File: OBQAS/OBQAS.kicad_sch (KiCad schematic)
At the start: 41 parts

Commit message: continued schematic editing
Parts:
- removed U?: Pico, RPi_Pico:RPi_Pico_SMD_TH, symbol MCU_RaspberryPi_and_Boards:Pico
- added C?: 220u, symbol Device:C_Polarized
- added C?: 100p, symbol Device:C
- added C? (x2): 10u, symbol Device:C
- added C?: 100n, symbol Device:C
- added D? (x4): 1N4001, Diode_THT:D_DO-41_SOD81_P10.16mm_Horizontal, symbol Diode:1N4001
- added J?: CH2, symbol Connector:Conn_01x02_Female
- added J?: CH1, symbol Connector:Conn_01x02_Female
- added J?: USB_C_Receptacle_USB2.0, symbol Connector:USB_C_Receptacle_USB2.0
- added K? (x4): G5NB-1A-E_DC5, RELAY_G5NB-1A DC5_OMR, symbol 2022-01-22_12-19-34:G5NB-1A-E_DC5
- added Q? (x4): IRLML2803TRPBF, SOT95P237X112-3N, symbol IRLML2803TRPBF:IRLML2803TRPBF
- added Q? (x2): BC846, Package_TO_SOT_SMD:SOT-23, symbol Transistor_BJT:BC846
- added R? (x14): 10k, symbol Device:R
- added R?: 1k, symbol Device:R
- added R? (x2): 50k, symbol Device:R
- added R? (x4): 100k, symbol Device:R
- added R? (x6): 470, symbol Device:R
- added R?: 5.1k(NC), symbol Device:R
- added R?: 1M, symbol Device:R
- added R?: 100mOhm, symbol Device:R
- added R? (x4): 2k, symbol Device:R
- added R? (x2): 10mOhm, symbol Device:R
- added R? (x2): 5.1k, symbol Device:R
- added R?: 0, symbol Device:R
- added SW?: SW_SPDT, symbol Switch:SW_SPDT
- added U? (x6): LM358, symbol Amplifier_Operational:LM358
- added U?: ESP32-WROOM-32, RF_Module:ESP32-WROOM-32, symbol RF_Module:ESP32-WROOM-32
- added U?: ADS1115IDGS, Package_SO:TSSOP-10_3x3mm_P0.5mm, symbol Analog_ADC:ADS1115IDGS
- added U?: AMS1117-3.3, Package_TO_SOT_SMD:SOT-223-3_TabPin2, symbol Regulator_Linear:AMS1117-3.3
- added U?: CH340C, Package_SO:SOIC-16_3.9x9.9mm_P1.27mm, symbol Interface_USB:CH340C
- added U?: ESP32-S2-WROVER-I, RF_Module:ESP32-S2-WROVER, symbol RF_Module:ESP32-S2-WROVER-I
- added U?: MCP4921, symbol Analog_DAC:MCP4921
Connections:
- net EN: now also C?.1, Q?.3 (C), R?.1, U?.3 (EN)
- net GND: now also U?.2 (GND), C?.1, C?.2, C?.2, C?.2, C?.2, D?.2 (A), D?.2 (A), D?.2 (A), D?.2 (A), J?.2 (Pin_2), J?.2 (Pin_2), J?.A1 (GND), J?.A12 (GND), J?.B1 (GND), J?.B12 (GND), J?.S1 (SHIELD), K?.1, K?.1, K?.4, K?.4, Q?.2, Q?.2, Q?.2, Q?.2, R?.1, R?.1, R?.1, R?.1, R?.1, R?.1, R?.1, R?.1, R?.2, R?.2, R?.2, R?.2, U?.1 (GND), U?.1 (GND), U?.1 (GND), U?.15 (GND), U?.3 (GND), U?.38 (GND), U?.39 (GND), U?.4 (V-), U?.4 (V-), U?.7 (Vss)
- net SCL: now also U?.10 (SCL)
- net SDA: now also U?.9 (SDA)
- net TPS_OUT: now also K?.3, K?.3
- net VCC: now also U?.1 (VI), SW?.1 (A); no longer J?.1
- net at Q?.1 (G): now also R?.2, R?.2
- net LOAD_IN: now reaches Q?.2 (D)
- net LOAD_IN: now also K?.3, K?.3
- net at Q?.3 (S): now also R?.2, R?.2
- net +5V: now reaches U?.3 (VO)
- net +5V: now also C?.1, J?.A4 (VBUS), J?.A9 (VBUS), J?.B4 (VBUS), J?.B9 (VBUS), R?.1, U?.16 (VCC), U?.3 (VI), U?.8 (V+), U?.8 (V+), U?.8 (VDD)
- new net: Q?.1, R?.2, R?.2 (x4)
- new net: Q?.2 (E), R?.1, U?.13 (~{DTR})
- new net: Q?.1 (B), R?.2 (x2)
- new net: R?.1, R?.1, U?.2 (-)
- new net: R?.1, R?.2, U?.1
- new net: R?.2, R?.2, R?.2, U?.3 (+)
- new net: K?.2, K?.2, R?.1, R?.2, R?.2 (x2)
- new net: J?.1 (Pin_1), R?.2, R?.2 (x2)
- new net: R?.1, R?.2, U?.3 (+)
- new net: J?.1, SW?.2 (B)
- new net: R?.1, R?.2, U?.2 (-)
- new net: R?.1, R?.1, U?.8 (Vout)
- new net: R?.1, R?.2, U?.5 (+)
- new net: J?.A5 (CC1), R?.1
- new net: R?.1, R?.2, U?.6 (-)
- new net: Q?.2 (E), R?.1, U?.14 (~{RTS})
- new net: R?.1, U?.2 (TXD)
- new net: J?.A6 (D+), J?.B6 (D+), U?.5 (UD+)
- new net: J?.A7 (D-), J?.B7 (D-), U?.6 (UD-)
- new net: U?.1 (GND), U?.26 (GND), U?.42 (GND), U?.43 (GND)
- new net: J?.B5 (CC2), R?.1
- new net +2V5: R?.1, R?.1, R?.1, R?.2
- new net +3V3: C?.1, C?.1, C?.2, R?.2, R?.2, U?.1 (Vdd), U?.2 (VDD), U?.2 (VO), U?.4 (V3), U?.6 (Vref)
- new net CH1R1: D?.1 (K), K?.4, Q?.3
- new net CH1R1_SIG: R?.1
- new net CH1R2: D?.1 (K), K?.1, Q?.3
- new net CH1R2_SIG: R?.1
- new net CH1_ADC_I: R?.1, U?.6 (AIN2), U?.7
- new net CH1_ADC_V: R?.1, R?.1, U?.4 (AIN0)
- new net CH2R1: D?.1 (K), K?.4, Q?.3
- new net CH2R1_SIG: R?.1
- new net CH2R2: D?.1 (K), K?.1, Q?.3
- new net CH2R2_SIG: R?.1
- new net CH2_ADC_I: R?.1, U?.1, U?.7 (AIN3)
- new net CH2_ADC_V: R?.1, R?.2, U?.5 (AIN1)
- new net IO0: Q?.3 (C), R?.1, U?.25 (IO0)
- new net RX: U?.3 (RXD)
- new net TX: R?.2
- no-connect marks 0 -> 7
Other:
- moved on the sheet: U?

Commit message: Finished schematic
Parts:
- removed U?: ESP32-S2-WROVER-I, RF_Module:ESP32-S2-WROVER, symbol RF_Module:ESP32-S2-WROVER-I
- added C19, C20: 100n, Capacitor_SMD:C_0805_2012Metric_Pad1.18x1.45mm_HandSolder, symbol Device:C
- added D1: LED, LED_SMD:LED_1206_3216Metric_Pad1.42x1.75mm_HandSolder, symbol Device:LED
- added DISP1: LCD, LCD:LCD-20x4, symbol Connector:Conn_01x04_Female
- added J3: K type, TerminalBlock:TerminalBlock_Altech_AK300-2_P5.00mm, symbol Connector:Screw_Terminal_01x02
- added J5: Micro_SD_Card, symbol Connector:Micro_SD_Card
- added R15: 1k, symbol Device:R
- added R20, R21, R22: 10k, symbol Device:R
- added R35, R40, R46, R52, R58: 49.9k, symbol Device:R
- added R9: 470, symbol Device:R
- added TP1: SENS_VP, symbol Connector:TestPoint
- added TP10: SCL, symbol Connector:TestPoint
- added TP11: SDA, symbol Connector:TestPoint
- added TP2: SENS_VN, symbol Connector:TestPoint
- added TP3: +5V, symbol Connector:TestPoint
- added TP4: +3V3, symbol Connector:TestPoint
- added TP5: IO0, symbol Connector:TestPoint
- added TP6: EN, symbol Connector:TestPoint
- added TP7: RX, symbol Connector:TestPoint
- added TP8: TX, symbol Connector:TestPoint
- added TP9: ADC_READY, symbol Connector:TestPoint
- C1, C15, C16, C18, C2, C8: renamed from C?; footprint (none) -> Capacitor_SMD:C_1206_3216Metric_Pad1.33x1.80mm_HandSolder
- C10, C11, C13, C14, C17, C4, C5, C9: renamed from C?; footprint (none) -> Capacitor_SMD:C_0805_2012Metric_Pad1.18x1.45mm_HandSolder
- C12: renamed from C?; footprint (none) -> Capacitor_SMD:C_1210_3225Metric_Pad1.33x2.70mm_HandSolder
- C3: renamed from C?; footprint (none) -> Capacitor_SMD:CP_Elec_6.3x9.9
- C6: renamed from C?; footprint (none) -> Capacitor_SMD:CP_Elec_10x10
- C7: renamed from C?; footprint (none) -> Capacitor_SMD:CP_Elec_8x6.9
- J1: renamed from J?; footprint (none) -> Connector_AMASS:AMASS_XT60-F_1x02_P7.20mm_Vertical
- J2: renamed from J?; footprint (none) -> Connector_USB:USB_C_Receptacle_Palconn_UTC16-G
- K1, K2, K3, K4: renamed from K?; footprint RELAY_G5NB-1A DC5_OMR -> (none)
- Q1, Q2, Q3, Q4: renamed from Q?; footprint SOT95P237X112-3N -> (none)
- U5: renamed from U?; footprint RPM0026A-MFG -> (none)
- gave numbers to parts that had none: 80
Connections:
- net +2V5: now also U6.5 (+)
- net +3V3: now also C20.2, J5.4 (VDD), R20.2, R21.2, R22.2, R35.2, R40.2, R46.2, R52.2, R58.2, TP4.1
- net +5V: now also C19.1, DISP1.2 (Pin_2), TP3.1
- net CH1R1_SIG: now also U3.9 (IO33)
- net CH1R2_SIG: now also U3.8 (IO32)
- net CH2R1_SIG: now also U3.12 (IO27)
- net CH2R2_SIG: now also U3.11 (IO26)
- net EN: now also TP6.1
- net GND: now also U3.4 (SENSOR_VP), U9.1 (ADDR), C19.2, C20.1, D1.1 (K), DISP1.1 (Pin_1), J3.2 (Pin_2), J5.6 (VSS), J5.9 (SHIELD), TP1.1
- net IO0: now also TP5.1
- net RX: now also U3.35 (TXD0/IO1), TP7.1
- net SCL: now also U3.36 (IO22), DISP1.4 (Pin_4), R20.1, TP10.1
- net SDA: now also U3.33 (IO21), DISP1.3 (Pin_3), R21.1, TP11.1
- net TX: now also U3.34 (RXD0/IO3), TP8.1
- net at U6.6 (-): now also U6.7
- net HSPI_CLK: now reaches U3.13 (IO14)
- net HSPI_CLK: now also U8.3 (SCK)
- net HSPI_MOSI: now reaches U3.16 (IO13)
- net HSPI_MOSI: now also U8.4 (SDI)
- net HSPI_CS: now reaches U3.23 (IO15)
- net HSPI_CS: now also U8.2 (~{CS})
- net at U3.24 (IO2): now also R9.1
- net ADC_READY: now reaches U3.26 (IO4)
- net ADC_READY: now also U9.2 (ALERT/RDY), R22.1, TP9.1
- net DAC_LDAC: now reaches U3.27 (IO16)
- net DAC_LDAC: now also U8.5 (~{LDAC})
- net SD_SS: now reaches U3.29 (IO5)
- net SD_SS: now also J5.2 (DAT3/CD), R40.1
- net SD_CLK: now reaches U3.30 (IO18)
- net SD_CLK: now also J5.5 (CLK)
- net SD_MISO: now reaches U3.31 (IO19)
- net SD_MISO: now also J5.7 (DAT0), R52.1
- net SD_MOSI: now reaches U3.37 (IO23)
- net SD_MOSI: now also J5.3 (CMD), R46.1
- net TC_-: now reaches U3.5 (SENSOR_VN)
- net TC_-: now also R15.1, TP2.1
- new net: D1.2 (A), R9.2
- new net: J3.1 (Pin_1), R15.2
- new net: J5.8 (DAT1), R58.1
- new net: J5.1 (DAT2), R35.1
- no-connect marks 7 -> 19
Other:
- moved on the sheet: C2, C4, C5, J2, Q1, Q2, Q3, Q4, Q5, Q6, Q9, R1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

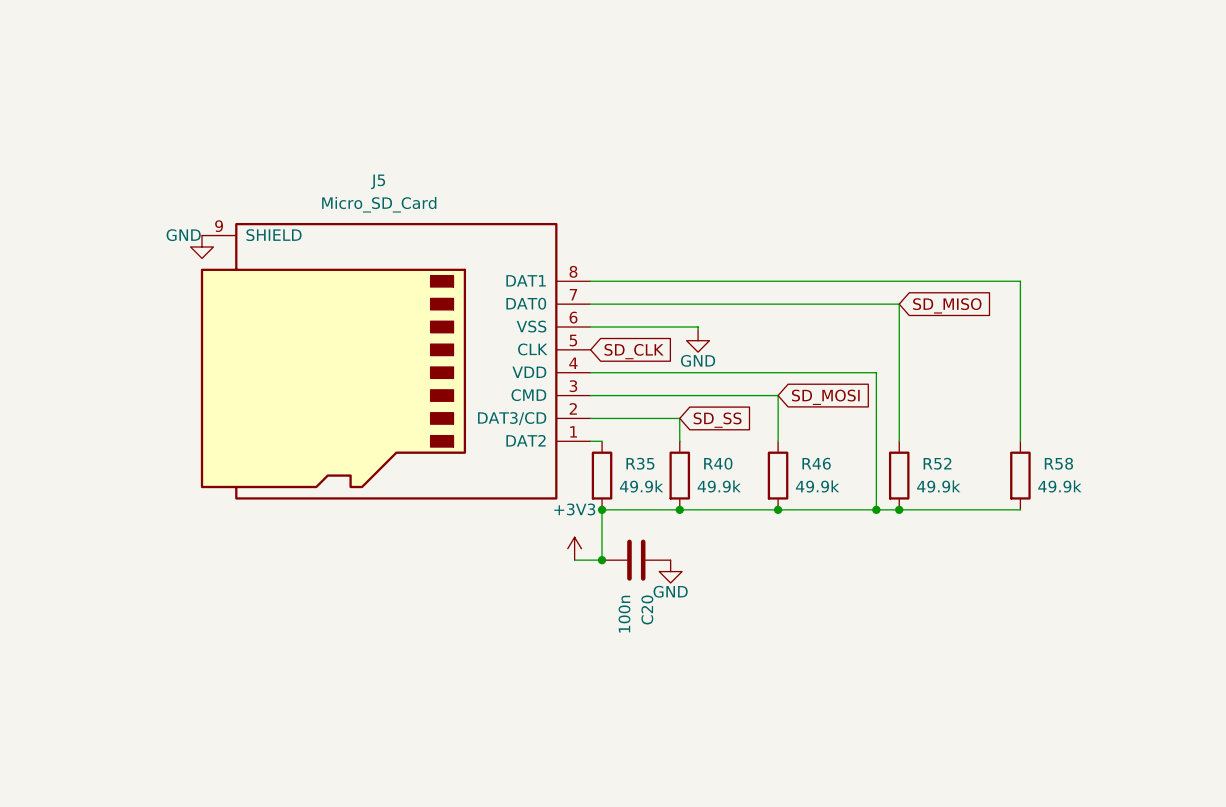
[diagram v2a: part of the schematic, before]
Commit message: changed SD card
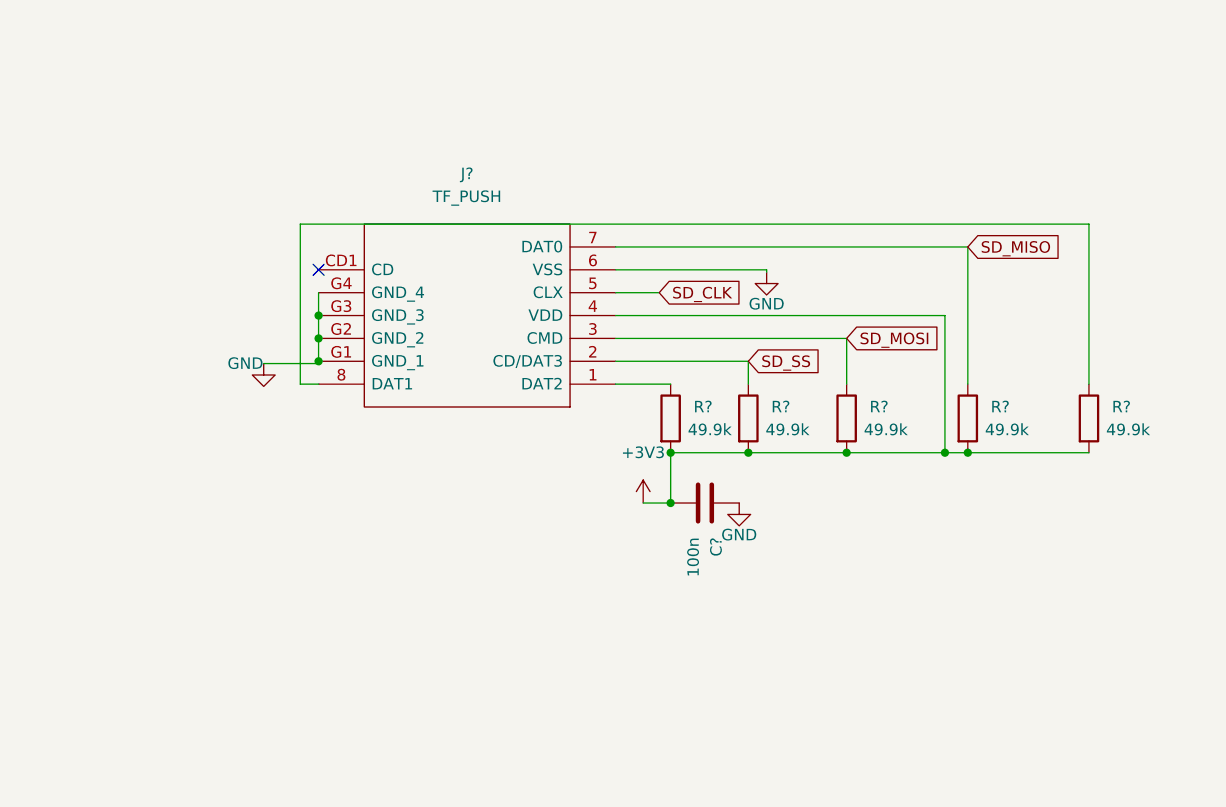
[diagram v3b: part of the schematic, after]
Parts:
- removed C20: 100n, Capacitor_SMD:C_0805_2012Metric_Pad1.18x1.45mm_HandSolder, symbol Device:C
- removed J5: Micro_SD_Card, symbol Connector:Micro_SD_Card
- removed R35, R40, R46, R52, R58: 49.9k, symbol Device:R
- added C?: 100n, Capacitor_SMD:C_0805_2012Metric_Pad1.18x1.45mm_HandSolder, symbol Device:C
- added J?: TF_PUSH, TFPUSH, symbol TF_PUSH:TF_PUSH
- added R? (x5): 49.9k, symbol Device:R
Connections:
- net +3V3: now also C?.2, J?.4 (VDD), R?.2, R?.2, R?.2, R?.2, R?.2
- net GND: now also C?.1, J?.6 (VSS), J?.G1 (GND_1), J?.G2 (GND_2), J?.G3 (GND_3), J?.G4 (GND_4)
- net SD_CLK: now also J?.5 (CLX)
- net SD_MISO: now also J?.7 (DAT0), R?.1
- net SD_MOSI: now also J?.3 (CMD), R?.1
- net SD_SS: now also J?.2 (CD/DAT3), R?.1
- new net: J?.8 (DAT1), R?.1
- new net: J?.1 (DAT2), R?.1
- no-connect marks 19 -> 20

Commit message: added encoder and assigned some footprints
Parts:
- added R? (x3): 10k, Resistor_SMD:R_0805_2012Metric_Pad1.20x1.40mm_HandSolder, symbol Device:R
- added SW2: Enc, symbol Device:RotaryEncoder_Switch
- J5: renamed from J?; footprint TFPUSH -> SD:TFPUSH
- J6, J7: footprint (none) -> TerminalBlock:TerminalBlock_Altech_AK300-2_P5.00mm
- JP1: footprint (none) -> Jumper:SolderJumper-3_P1.3mm_Bridged12_RoundedPad1.0x1.5mm
- K1, K2, K3, K4: footprint (none) -> footprints:G5NB-1A-E DC5
- L1: value L_Iron -> 4.7uH; footprint (none) -> Inductor_THT:L_Radial_D29.8mm_P29.30mm_Murata_1400series
- Q1, Q2, Q3, Q4: footprint (none) -> Package_TO_SOT_SMD:SOT-23
- Q7, Q8: footprint Package_TO_SOT_THT:TO-220-3_Vertical -> Package_TO_SOT_THT:TO-220F-3_Horizontal_TabDown
- Q9: footprint Package_TO_SOT_THT:TO-247-3_Vertical -> Package_TO_SOT_THT:TO-247-3_Horizontal_TabDown
- R1, R10, R11, R12, R13, R14, R15, R16, R17, R18, R19, R2, R20, R21, R22, R23, R24, R25, R26, R27, R28, R29, R3, R30, R31, R33, R34, R36, R37, R38, R39, R4, R41, R42, R43, R44, R45, R47, R49, R5, R50, R51, R53, R54, R55, R56, R57, R6, R7, R8, R9: footprint (none) -> Resistor_SMD:R_0805_2012Metric_Pad1.20x1.40mm_HandSolder
- R32, R48: footprint (none) -> Resistor_SMD:R_2512_6332Metric_Pad1.40x3.35mm_HandSolder
- R35, R40, R46, R52, R58: renamed from R?; footprint (none) -> Resistor_SMD:R_0805_2012Metric_Pad1.20x1.40mm_HandSolder
- R59: footprint (none) -> Resistor_THT:R_Axial_Power_L20.0mm_W6.4mm_P30.48mm
- gave numbers to parts that had none: 1
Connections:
- net +3V3: now also R?.2, R?.2, SW2.S1
- net GND: now also R?.1, SW2.C
- net ENC_B: now reaches U3.10 (IO25)
- net ENC_B: now also R?.1, SW2.B
- net ENC_Button: now reaches U3.14 (IO12)
- net ENC_Button: now also R?.2, SW2.S2
- net ENC_A: now reaches U3.28 (IO17)
- net ENC_A: now also R?.1, SW2.A
- no-connect marks 20 -> 17
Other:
- moved on the sheet: C20, J5, R35, R40, R46, R52, R58

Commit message: beginning of PCB layout
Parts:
- removed SW1: SW_SPDT, symbol Switch:SW_SPDT
- added C21: 220u, Capacitor_SMD:CP_Elec_6.3x9.9, symbol Device:C_Polarized
- added F1: Fuse, Fuse:Fuse_Blade_ATO_directSolder, symbol Device:Fuse
- added SW1: SW_SPST, TerminalBlock:TerminalBlock_Altech_AK300-2_P5.00mm, symbol Switch:SW_SPST
- D2, D3, D4, D5: footprint Diode_THT:D_DO-41_SOD81_P10.16mm_Horizontal -> Diode_SMD:D_SOD-123
- K1, K2, K3, K4: footprint footprints:G5NB-1A-E DC5 -> relay:G5NB-1A-E DC5
- Q7, Q8: footprint Package_TO_SOT_THT:TO-220F-3_Horizontal_TabDown -> Package_TO_SOT_THT:TO-220F-3_Horizontal_TabUp
- Q9: footprint Package_TO_SOT_THT:TO-247-3_Horizontal_TabDown -> Package_TO_SOT_THT:TO-247-3_Horizontal_TabUp
- R36: footprint Resistor_SMD:R_0805_2012Metric_Pad1.20x1.40mm_HandSolder -> Resistor_SMD:R_2512_6332Metric_Pad1.40x3.35mm_HandSolder
- SW2: footprint (none) -> Rotary_Encoder:RotaryEncoder_Alps_EC11E-Switch_Vertical_H20mm_CircularMountingHoles
- TP1, TP10, TP11, TP12, TP13, TP14, TP15, TP16, TP17, TP18, TP19, TP2, TP20, TP3, TP4, TP5, TP6, TP7, TP8, TP9: footprint (none) -> TestPoint:TestPoint_Pad_D2.5mm
- U5: footprint (none) -> TPS_IC:TPS55288QWRPMRQ1
- U6, U7, U8: footprint (none) -> Package_SO:SO-8_3.9x4.9mm_P1.27mm
- gave numbers to parts that had none: 3
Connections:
- net +5V: now also C21.1
- net GND: now also C21.2
- net VCC: now also F1.2
- net at J1.1: now also SW1.2 (B)
- new net: F1.1, SW1.1 (A)
- no-connect marks 17 -> 16

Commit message: inital routing complete
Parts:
- removed D1: LED, LED_SMD:LED_1206_3216Metric_Pad1.42x1.75mm_HandSolder, symbol Device:LED
- removed R9: 470, Resistor_SMD:R_0805_2012Metric_Pad1.20x1.40mm_HandSolder, symbol Device:R
- added C22: 100n, Capacitor_SMD:C_0805_2012Metric_Pad1.18x1.45mm_HandSolder, symbol Device:C
- added H1, H2, H3, H4: MountingHole, MountingHole:MountingHole_3.2mm_M3, symbol Mechanical:MountingHole
- R5, R6: value 10k -> 470
- TP15: footprint TestPoint:TestPoint_Pad_D2.5mm -> TestPoint:TestPoint_Pad_D1.0mm
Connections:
- net +3V3: now also C22.1
- net +5V: now also D2.1 (K), D3.1 (K), D4.1 (K), D5.1 (K), K1.1, K2.4, K3.1, K4.4
- net CH1R1: now also D2.2 (A); no longer D2.1 (K)
- net CH1R2: now also D3.2 (A); no longer D3.1 (K)
- net CH2R1: now also D4.2 (A); no longer D4.1 (K)
- net CH2R2: now also D5.2 (A); no longer D5.1 (K)
- net EN: no longer R25.1
- net GND: now also C22.2; no longer D2.2 (A), D3.2 (A), D4.2 (A), D5.2 (A), K1.1, K2.4, K3.1, K4.4
- net EN_UVLDO: now reaches U3.24 (IO2)
- net EN_UVLDO: now also R25.1
- net D+: now reaches J2.A6 (D+), J2.B6 (D+), U4.5 (UD+)
- net D-: now reaches J2.A7 (D-), J2.B7 (D-), U4.6 (UD-)
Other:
- moved on the sheet: D2, D3, D4, D5

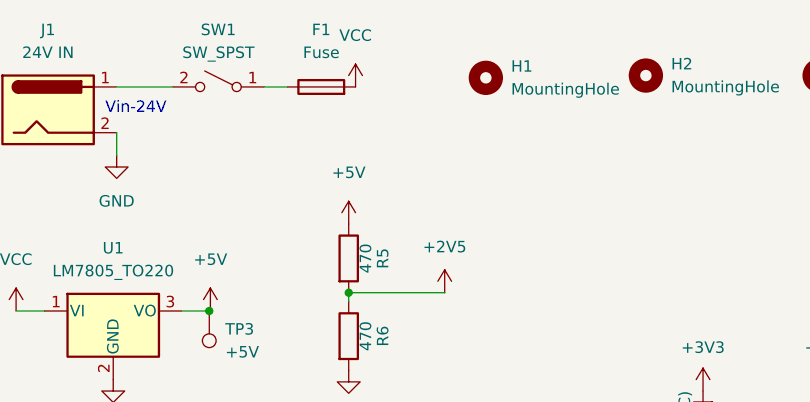
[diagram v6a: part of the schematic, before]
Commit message: finished layout, doing silkscreen adjustment
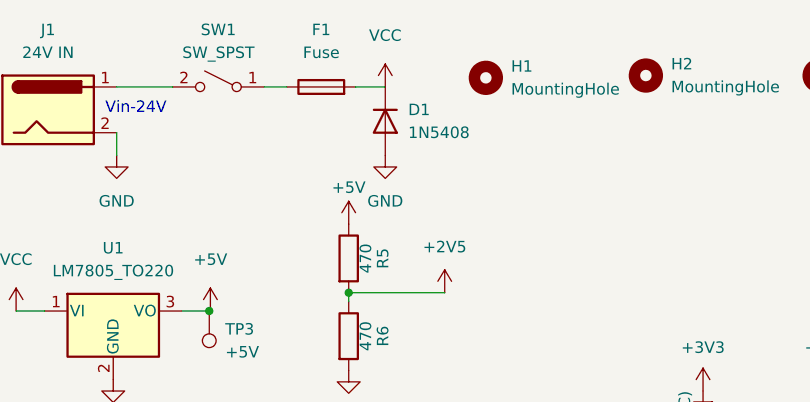
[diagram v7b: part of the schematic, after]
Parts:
- added D1: 1N5408, Diode_THT:D_DO-201AD_P15.24mm_Horizontal, symbol Diode:1N5408
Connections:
- net GND: now also D1.2 (A)
- net VCC: now also D1.1 (K)
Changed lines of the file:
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@@
     (stroke (width 0) (type default) (color 0 0 0 0))
   )
+  (wire (pts (xy 63.5 24.13) (xy 60.198 24.13))
+    (stroke (width 0) (type default) (color 0 0 0 0))
+  )
   (wire (pts (xy 319.532 309.88) (xy 356.108 309.88))
     (stroke (width 0) (type default) (color 0 0 0 0))
@@
     (pin "1")
   )
+  (symbol (lib_id "Diode:1N5408") (at 63.5 27.94 270) (unit 1)
+    (in_bom yes) (on_board yes) (fields_autoplaced)
+    (property "Reference" "D1" (id 0) (at 66.04 26.6699 90)
+      (effects (font (size 1.27 1.27)) (justify left))
+    )
+    (property "Value" "1N5408" (id 1) (at 66.04 29.2099 90)
+      (effects (font (size 1.27 1.27)) (justify left))
+    )
+    (property "Footprint" "Diode_THT:D_DO-201AD_P15.24mm_Horizontal" (id 2) (at 59.055 27.94 0)
+      (effects (font (size 1.27 1.27)) hide)
+    )
+    (property "Datasheet" "http://www.vishay.com/docs/88516/1n5400.pdf" (id 3) (at 63.5 27.94 0)
+      (effects (font (size 1.27 1.27)) hide)
+    )
+    (pin "1")
+    (pin "2")
+  )
   (symbol (lib_id "power:+3V3") (at 133.35 210.312 0) (mirror y) (unit 1)
     (in_bom yes) (on_board yes) (fields_autoplaced)
@@
     (pin "2")
   )
+  (symbol (lib_id "power:GND") (at 63.5 31.75 0) (unit 1)
+    (in_bom yes) (on_board yes) (fields_autoplaced)
+    (property "Reference" "#PWR050" (id 0) (at 63.5 38.1 0)
+      (effects (font (size 1.27 1.27)) hide)
+    )
+    (property "Value" "GND" (id 1) (at 63.5 36.83 0))
+    (property "Footprint" "" (id 2) (at 63.5 31.75 0)
+      (effects (font (size 1.27 1.27)) hide)
+    )
+    (property "Datasheet" "" (id 3) (at 63.5 31.75 0)
+      (effects (font (size 1.27 1.27)) hide)
+    )
+    (pin "1")
+  )
   (symbol (lib_id "power:+2V5") (at 496.062 167.64 0) (unit 1)
     (in_bom yes) (on_board yes)
@@
   )
   (symbol (lib_id "power:+5V") (at 59.436 39.37 0) (unit 1)
-    (in_bom yes) (on_board yes) (fields_autoplaced)
+    (in_bom yes) (on_board yes)
     (property "Reference" "#PWR011" (id 0) (at 59.436 43.18 0)
       (effects (font (size 1.27 1.27)) hide)
     )
-    (property "Value" "+5V" (id 1) (at 59.436 33.655 0))
+    (property "Value" "+5V" (id 1) (at 59.436 35.306 0))
     (property "Footprint" "" (id 2) (at 59.436 39.37 0)
       (effects (font (size 1.27 1.27)) hide)
@@
     (pin "2")
   )
-  (symbol (lib_id "power:VCC") (at 60.198 24.13 0) (unit 1)
+  (symbol (lib_id "power:VCC") (at 63.5 24.13 0) (unit 1)
     (in_bom yes) (on_board yes) (fields_autoplaced)
-    (property "Reference" "#PWR08" (id 0) (at 60.198 27.94 0)
+    (property "Reference" "#PWR08" (id 0) (at 63.5 27.94 0)
       (effects (font (size 1.27 1.27)) hide)
     )
-    (property "Value" "VCC" (id 1) (at 60.198 18.415 0))
-    (property "Footprint" "" (id 2) (at 60.198 24.13 0)
+    (property "Value" "VCC" (id 1) (at 63.5 18.415 0))
+    (property "Footprint" "" (id 2) (at 63.5 24.13 0)
       (effects (font (size 1.27 1.27)) hide)
     )
-    (property "Datasheet" "" (id 3) (at 60.198 24.13 0)
+    (property "Datasheet" "" (id 3) (at 63.5 24.13 0)
       (effects (font (size 1.27 1.27)) hide)
     )
@@
       (reference "#PWR049") (unit 1) (value "GND") (footprint "")
     )
+    (path "/42192181-be84-43cb-8f59-caa16460fae9"
+      (reference "#PWR050") (unit 1) (value "GND") (footprint "")
+    )
     (path "/cce8f13a-1a8e-42cc-9677-30bfd283cd7d"
       (reference "#PWR052") (unit 1) (value "GND") (footprint "")
@@
       (reference "C22") (unit 1) (value "100n") (footprint "Capacitor_SMD:C_0805_2012Metric_Pad1.18x1.45mm_HandSolder")
     )
+    (path "/17e8c067-290d-4cee-9625-906383d7553a"
+      (reference "D1") (unit 1) (value "1N5408") (footprint "Diode_THT:D_DO-201AD_P15.24mm_Horizontal")
+    )
     (path "/644ccf93-acd8-4393-8403-c9ffc137c4a0"
